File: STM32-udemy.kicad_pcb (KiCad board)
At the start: 2 copper layers, 66 x 26 mm, 31 parts, among them J1 USB_B_Micro, J2 Serial_Wire, J3 Conn_01x20_Male, J4 Conn_01x20_Male, SW1 SW_Push, SW2 SW_SPDT, U1 NCP1117, U2 STM32F446RCTx, Y1 Crystal_GND24

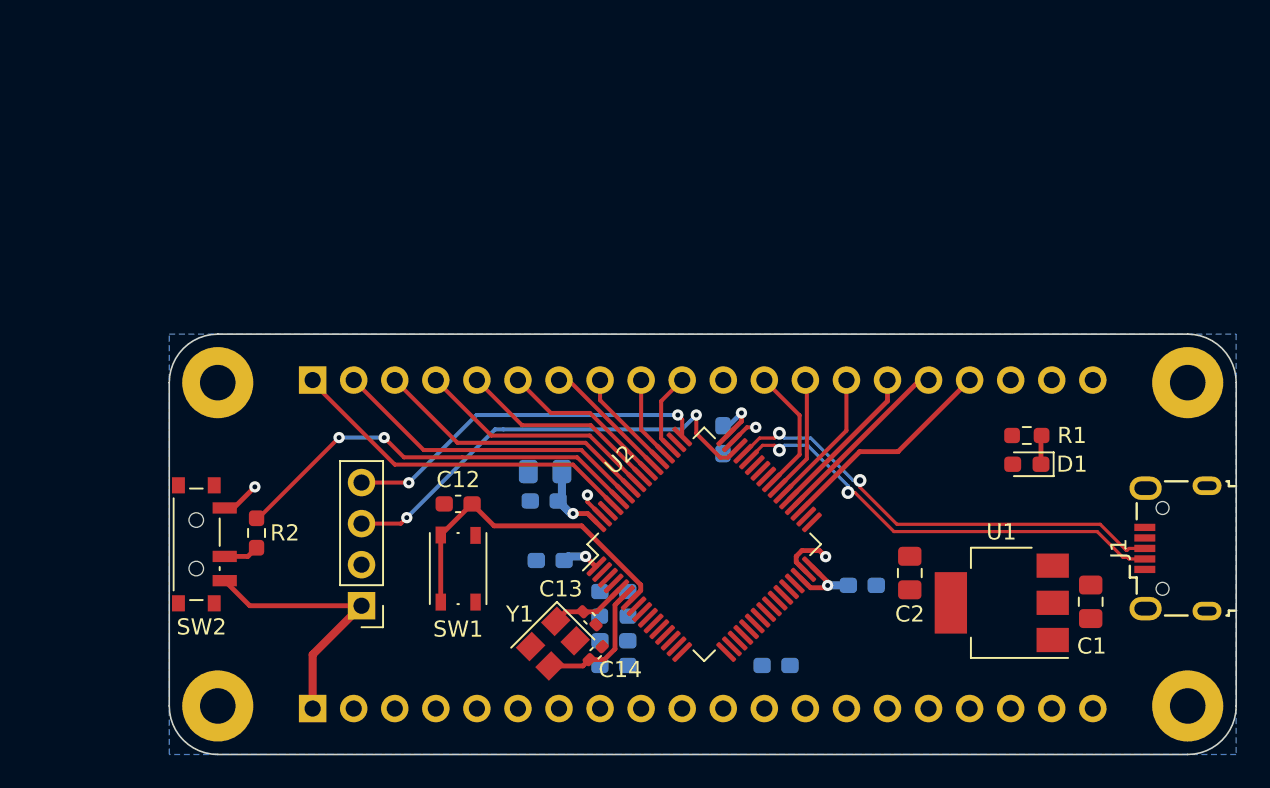
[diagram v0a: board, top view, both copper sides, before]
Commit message: Remove components that are not essential
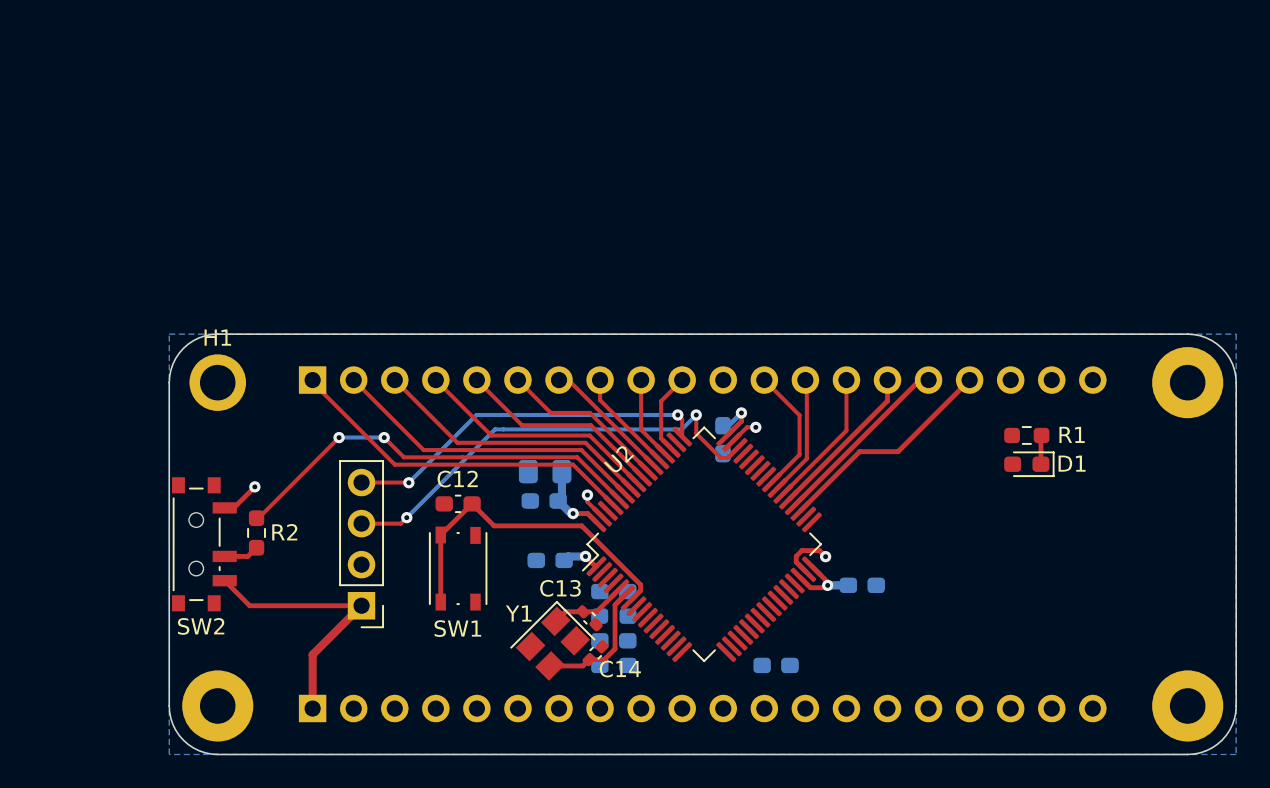
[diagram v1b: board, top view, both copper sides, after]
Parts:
- removed C1, C2: 10u, Capacitor_SMD:C_0805_2012Metric_Pad1.18x1.45mm_HandSolder
- removed J1: USB_B_Micro, Connector_USB:USB_Micro-B_Wuerth_629105150521
- removed U1: NCP1117, Package_TO_SOT_SMD:SOT-223-3_TabPin2
- H1: footprint MountingHole:MountingHole_2.2mm_M2_Pad -> MountingHole:MountingHole_2.2mm_M2_ISO7380_Pad
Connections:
- U2 pad 10: /PC2 -> unconnected-(U2-Pad10)
- U2 pad 11: /PC3 -> unconnected-(U2-Pad11)
- U2 pad 44: /USB_D- -> unconnected-(U2-Pad44)
- U2 pad 45: /USB_D+ -> unconnected-(U2-Pad45)
- U2 pad 8: /PC0 -> unconnected-(U2-Pad8)
- U2 pad 9: /PC1 -> unconnected-(U2-Pad9)
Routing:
- net /USB_D+: track 28.6 -> 0.00 mm, vias 2 -> 0
- net /USB_D-: track 28.3 -> 0.00 mm, vias 2 -> 0

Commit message: Initial board layout
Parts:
- removed C13, C14: C, Capacitor_SMD:C_0402_1005Metric_Pad0.74x0.62mm_HandSolder
- removed H1: MountingHole, MountingHole:MountingHole_2.2mm_M2_ISO7380_Pad
- removed H2, H3, H4: MountingHole, MountingHole:MountingHole_2.2mm_M2_Pad
- removed J4: Conn_01x20_Male, Connector_PinHeader_2.54mm:PinHeader_1x20_P2.54mm_Vertical
- removed U2: STM32F446RCTx, Package_QFP:LQFP-64_10x10mm_P0.5mm
- added C1: 10u, Capacitor_SMD:C_0805_2012Metric_Pad1.18x1.45mm_HandSolder, B.Cu at (104.4, 75.4)
- added C2: 100n, Capacitor_SMD:C_0603_1608Metric_Pad1.08x0.95mm_HandSolder, B.Cu at (104.4, 73.7)
- added J1: Conn_01x20_Male, Connector_PinHeader_2.54mm:PinHeader_1x20_P2.54mm_Vertical, B.Cu at (119.4, 58.4)
- added U1: STM32F446RCTx, Package_QFP:LQFP-64_10x10mm_P0.5mm, F.Cu at (97.8, 69.8)
- C10: value 1u -> 100n; moved to F.Cu
- C11: value 1u -> C; footprint Capacitor_SMD:C_0603_1608Metric_Pad1.08x0.95mm_HandSolder -> Capacitor_SMD:C_0402_1005Metric_Pad0.74x0.62mm_HandSolder; moved to F.Cu
- C12: value 100n -> C; footprint Capacitor_SMD:C_0603_1608Metric_Pad1.08x0.95mm_HandSolder -> Capacitor_SMD:C_0402_1005Metric_Pad0.74x0.62mm_HandSolder
- C3: value 10u -> 100n; footprint Capacitor_SMD:C_0805_2012Metric_Pad1.18x1.45mm_HandSolder -> Capacitor_SMD:C_0603_1608Metric_Pad1.08x0.95mm_HandSolder
- C8, C9: value 100n -> 1u
- J2: value Serial_Wire -> Conn_01x20_Male; footprint Connector_PinHeader_2.54mm:PinHeader_1x04_P2.54mm_Vertical -> Connector_PinHeader_2.54mm:PinHeader_1x20_P2.54mm_Vertical; moved to B.Cu
- J3: value Conn_01x20_Male -> Serial_Wire; footprint Connector_PinHeader_2.54mm:PinHeader_1x20_P2.54mm_Vertical -> Connector_PinHeader_2.54mm:PinHeader_1x04_P2.54mm_Vertical; moved to F.Cu
- moved R1 50.8 mm to (79.9, 72.8), turned to 0 degrees
- moved D1 50.5 mm to (80.0, 75.8), turned to 0 degrees
- moved SW2 44.7 mm to (119.6, 68.8), turned to 90 degrees
- moved C10 40.7 mm to (79.4, 62.9), turned to 0 degrees
- moved R2 38.0 mm to (118.8, 75.7), turned to 0 degrees
- moved C7 34.7 mm to (103.9, 62.0)
- moved J2 32.1 mm to (119.4, 81.3), turned to 90 degrees
- moved Y1 31.3 mm to (113.2, 64.9), turned to 0 degrees
- moved J3 28.2 mm to (71.1, 73.7), turned to 180 degrees
- moved C11 28.1 mm to (108.7, 62.6)
- moved C9 26.9 mm to (103.9, 66.5), turned to 0 degrees
- moved FB1 26.9 mm to (103.9, 65.0)
- moved SW1 26.3 mm to (80.0, 67.3), turned to 0 degrees
- moved C5 25.6 mm to (94.6, 61.6), turned to 180 degrees
- moved C6 25.4 mm to (107.3, 67.9), turned to 180 degrees
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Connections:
- C10 pad 1: +3.3VA -> /NRST
- C11 pad 1: +3V3 -> /HSE_IN
- C12 pad 1: /NRST -> /HSE_OUT
- C7 pad 1: +3V3 -> +3.3VA
- C8 pad 1: +3V3 -> +3.3VA
- C9 pad 1: +3.3VA -> +3V3
- J2 pad 1: +3V3 -> /PB8
- J2 pad 2: GND -> /PB7
- J2 pad 3: /SWDIO -> /PB6
- J2 pad 4: /SWCLK -> /PB5
- J3 pad 2: /PC13 -> GND
- J3 pad 3: /PC14 -> /SWDIO
- J3 pad 4: /PC15 -> /SWCLK
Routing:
- net +3V3: track 32.1 -> 0.00 mm, vias 4 -> 0
- net /SWDIO: track 28.1 -> 0.00 mm, vias 2 -> 0
- net /BOOT0: track 26.1 -> 0.00 mm, vias 2 -> 0
- net /SWCLK: track 22.8 -> 0.00 mm, vias 2 -> 0
- net /PB8: track 21.9 -> 0.00 mm
- net /NRST: track 20.6 -> 0.00 mm
- net /PB7: track 19.7 -> 0.00 mm
- net /PB6: track 17.4 -> 0.00 mm
- net /PB5: track 15.0 -> 0.00 mm
- net /PB14: track 13.8 -> 0.00 mm
- net /PB4: track 12.7 -> 0.00 mm
- net /PB15: track 11.5 -> 0.00 mm
- net /PB3: track 10.4 -> 0.00 mm
- net /PC6: track 9.91 -> 0.00 mm
- net GND: track 9.33 -> 0.00 mm, vias 4 -> 0
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- removed copper zone on B.Cu, net GND
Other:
- board size 66 x 26 mm -> 53.3 x 27.9 mm
